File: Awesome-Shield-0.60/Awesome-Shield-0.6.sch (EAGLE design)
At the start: 23 parts, among them SW1 SPST_TACT-EVQQ2, SW2 DPDT, U1 LIGHTSENSORTEMT6000

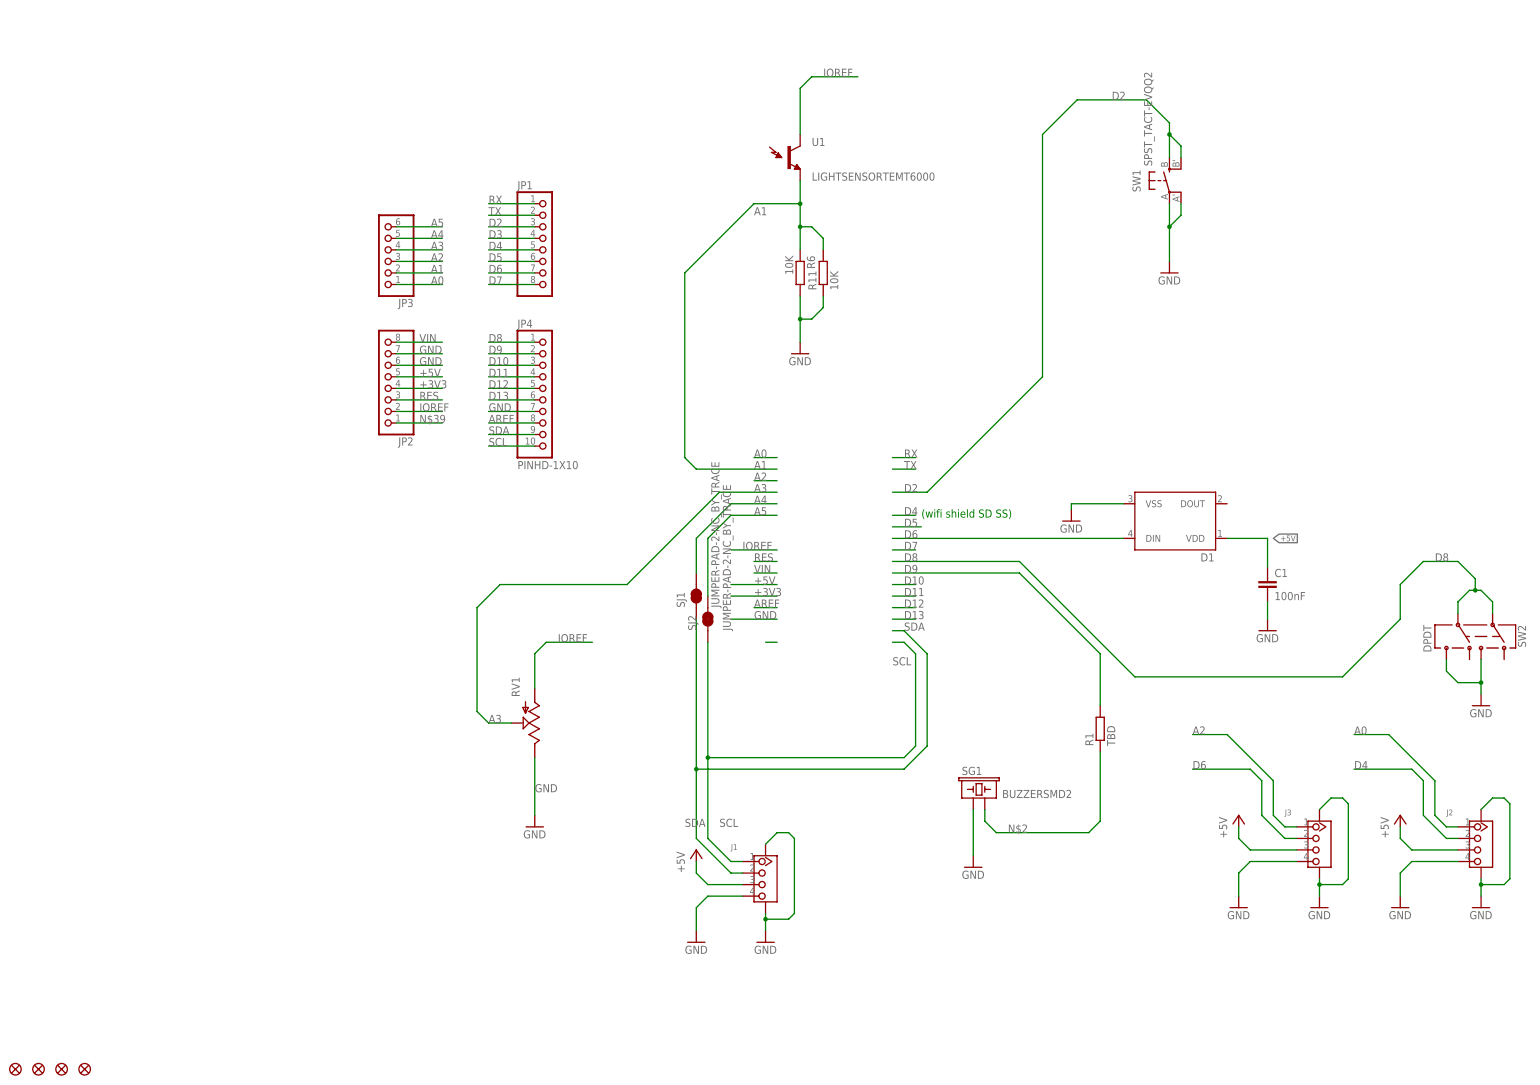
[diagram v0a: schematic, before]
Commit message: schematic cosmetics, change Rs to 1206 footprint
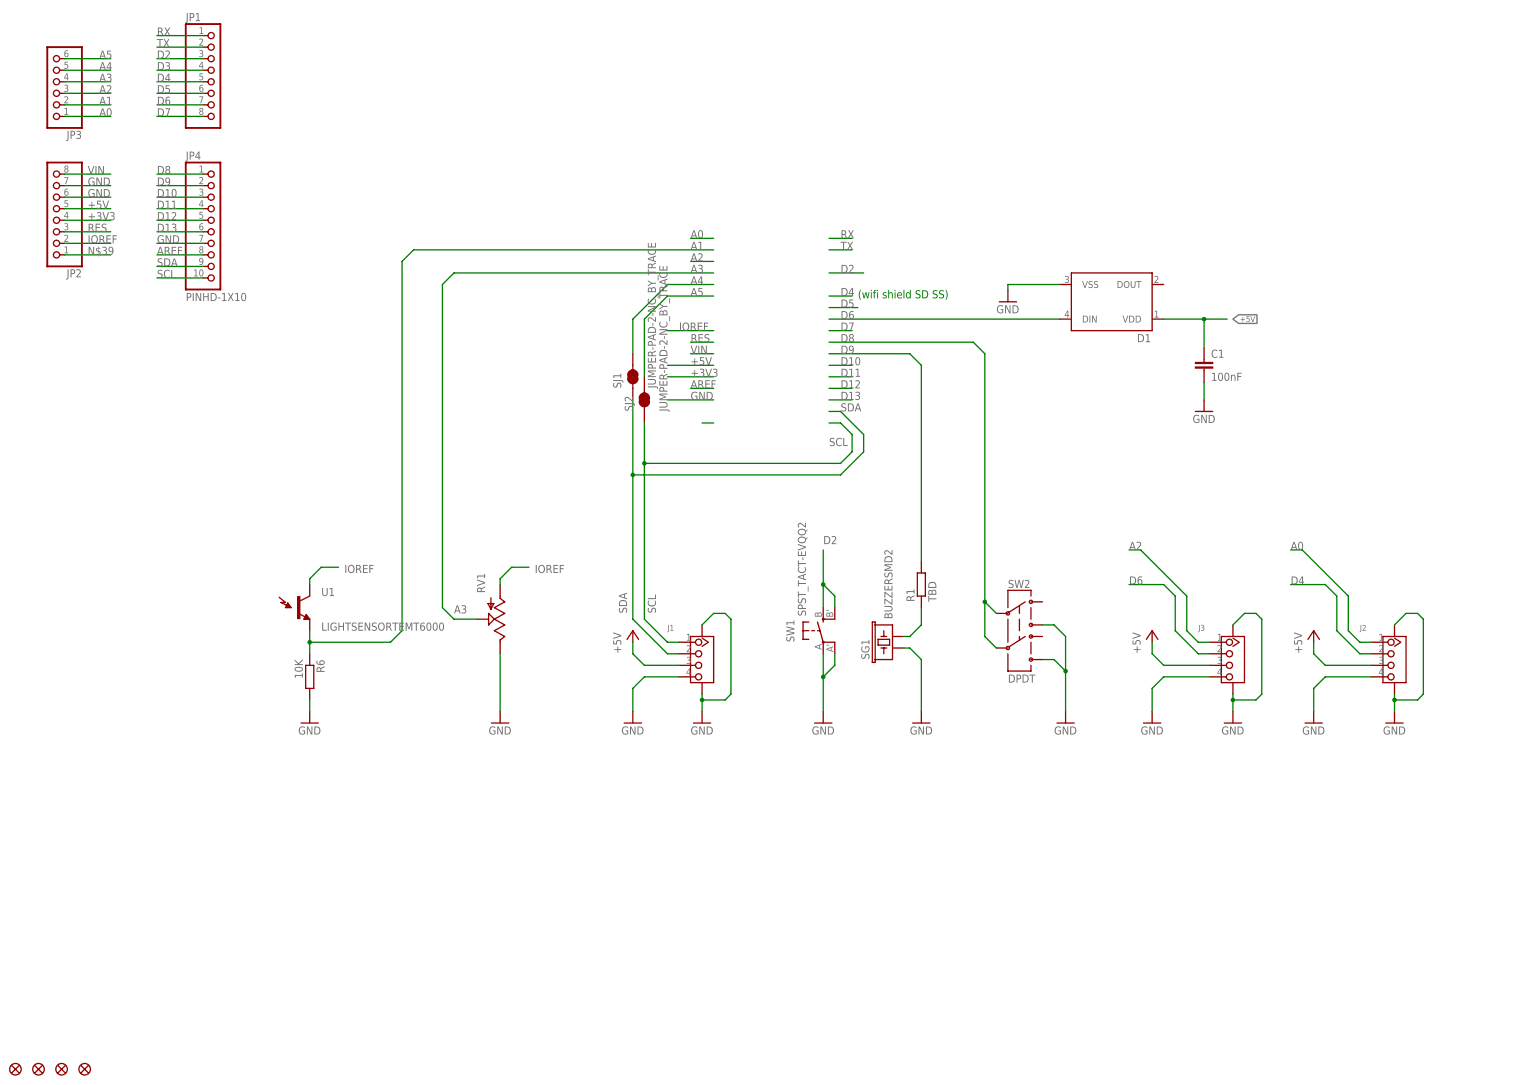
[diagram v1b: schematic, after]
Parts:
- removed R11: 10K, rcl:R-EU_R0603
- R1: device rcl:R-EU_R0603 -> rcl:R-EU_R1206
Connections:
- net A1: no longer R11.2
- net GND: no longer R11.1
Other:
- note added: "Power for the LED can be 3V3 ... 5V, forward voltage of blue and green emitters might be slightly above 3V3, so for full brightness the nominal current might not be reached with 3V3 for blue and green -> color temperature for full white is warm"
- moved on the sheet: C1, D1, J1, J2, J3, JP1, JP2, JP3, JP4, R1, R6, RV1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

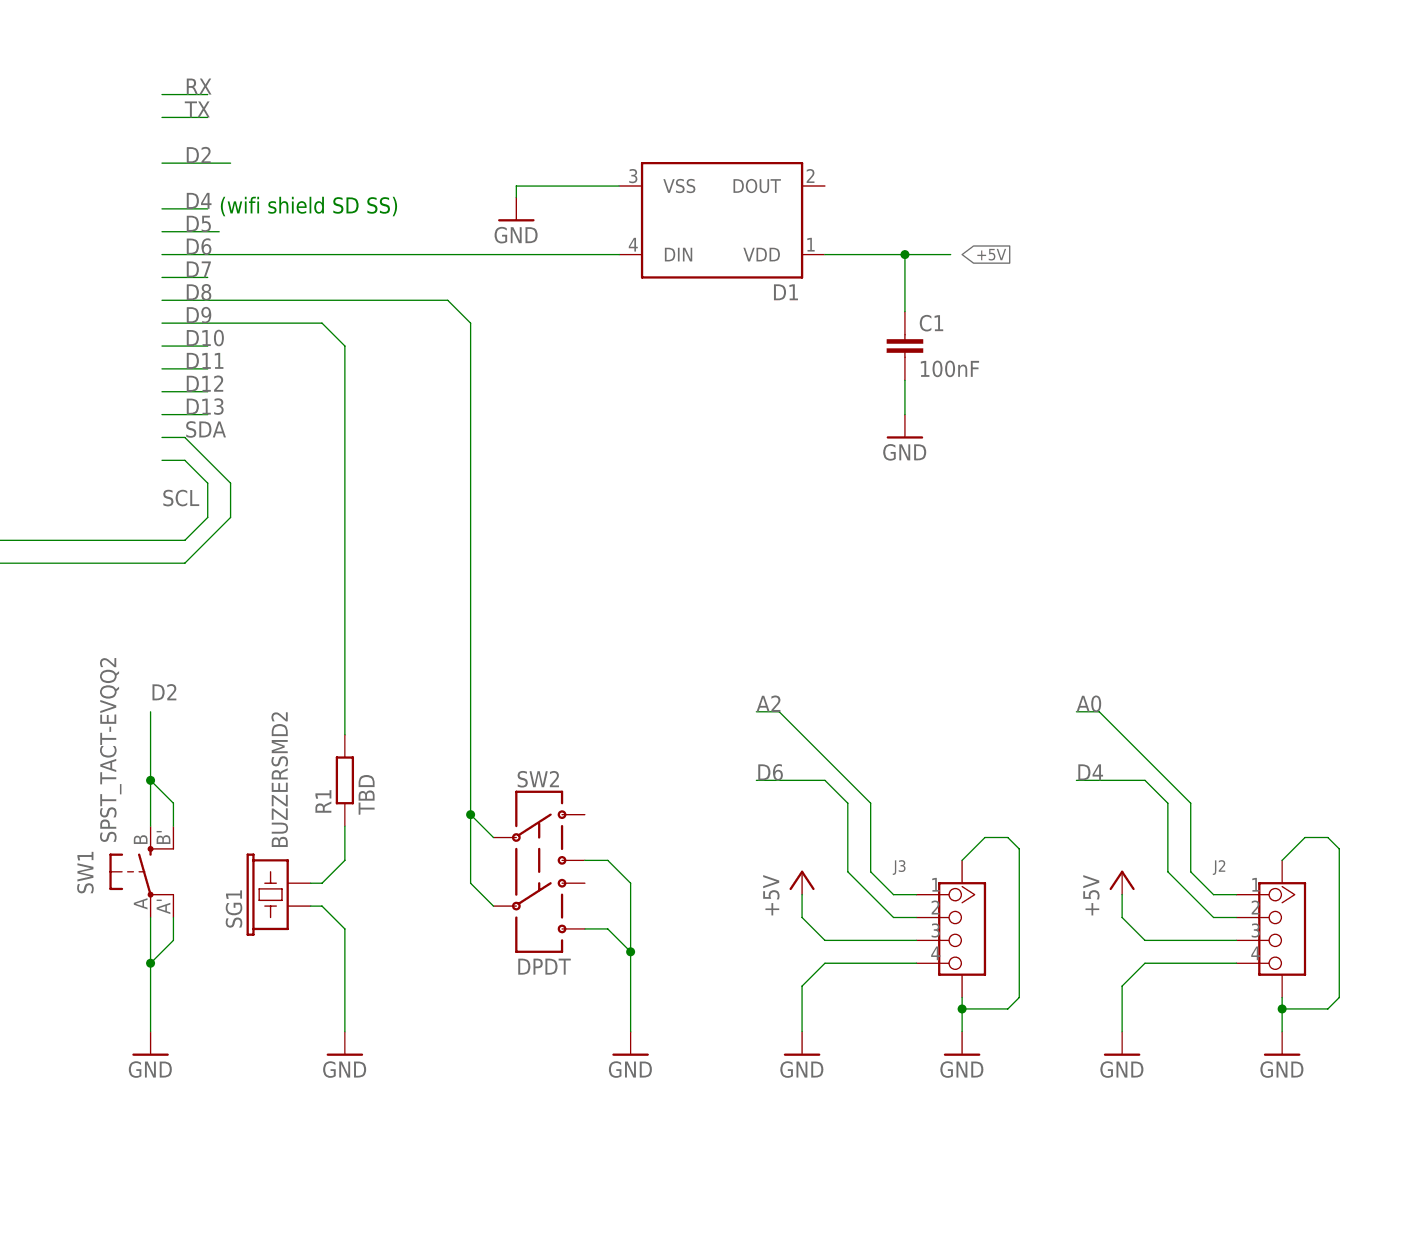
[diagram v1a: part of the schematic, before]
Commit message: change buzzer to Loudity t68-0808, sketch part
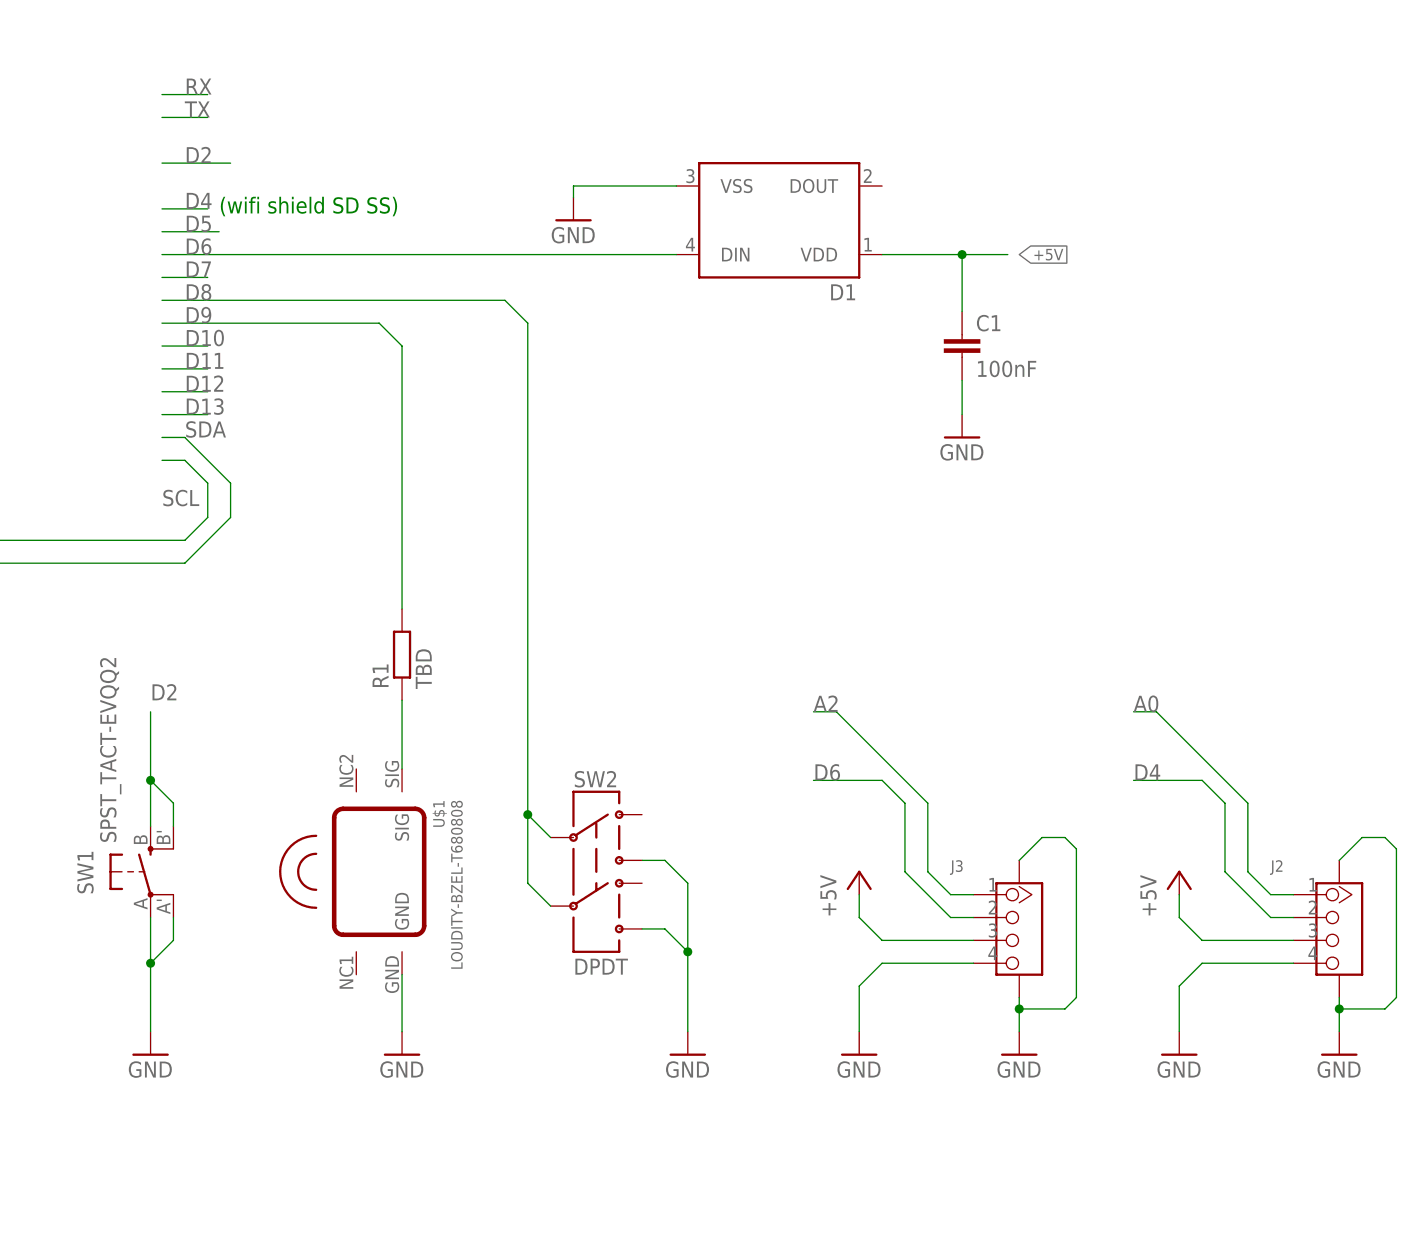
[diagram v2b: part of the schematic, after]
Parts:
- removed SG1: BUZZERSMD2, SparkFun-Electromechanical:BUZZERSMD2
- added U$1: LOUDITY-BZEL-T680808, buzzer-loudity-bzel-t68-0808:LOUDITY-BZEL-T680808
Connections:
- net GND: now also U$1.GND; no longer SG1.1
- net N$2: now also U$1.SIG; no longer SG1.2
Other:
- note added: "GROVE PORT1"
- note added: "GROVE PORT2"
- note added: "GROVE PORT3"
- moved on the sheet: C1, D1, J2, J3, R1, SW2
